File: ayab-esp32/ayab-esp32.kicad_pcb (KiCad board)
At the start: 4 copper layers, 285.1 x 48.1 mm, 237 parts, among them J201 SPARE1, J202 SPARE0, J401 900.965.CK35 SOLENOIDS A, J402 900.965.CK35 SOLENOIDS B, J403 910.950 SOLENOIDS A, J404 910.950 SOLENOIDS B, J405 910.950 ENCODERS EOL R, J406 930.940 SOLENOIDS A, J407 930.940 SOLENOIDS B, J408 910.950 EOL L, J409 930.940 EOL R, J410 930.940 ENCODERS, J411 900.965 EOL L, J412 900.965 EOL R, J413 900.965 ENCODERS, J414 930.940 EOL L, J501 USB_C_Receptacle_USB2.0, J601 VIN, J602 Brother_5P, J604 Brother_4R, J701 CTRL_3v3, J702 CTRL_5V, J801 AYAB_UART, J802 I2C_VBUS, J803 USER_I2C, J804 I2C_VBUS, J805 AYAB_SPI, J806 AYAB_I2C, Q201 AO3400A, Q501 BCM857BV, Q502 LP9435LT1G, Q801 AO3400A, Q802 AO3400A, Q803 AO3400A, Q804 AO3400A, Q805 LP9435LT1G, Q806 AO3400A, SW201 USER, SW202 RESET, SW203 BOOTSEL, U201 ESP32-S3-MINI-1, U301 MCP23017_SS, U302 ULN2003A, U303 ULN2003A, U304 ULN2003A, U403 LM66100DCKR, U501 SRV05-4, U601 XL1509, U602 XL1509, U701 SN74LVC4245

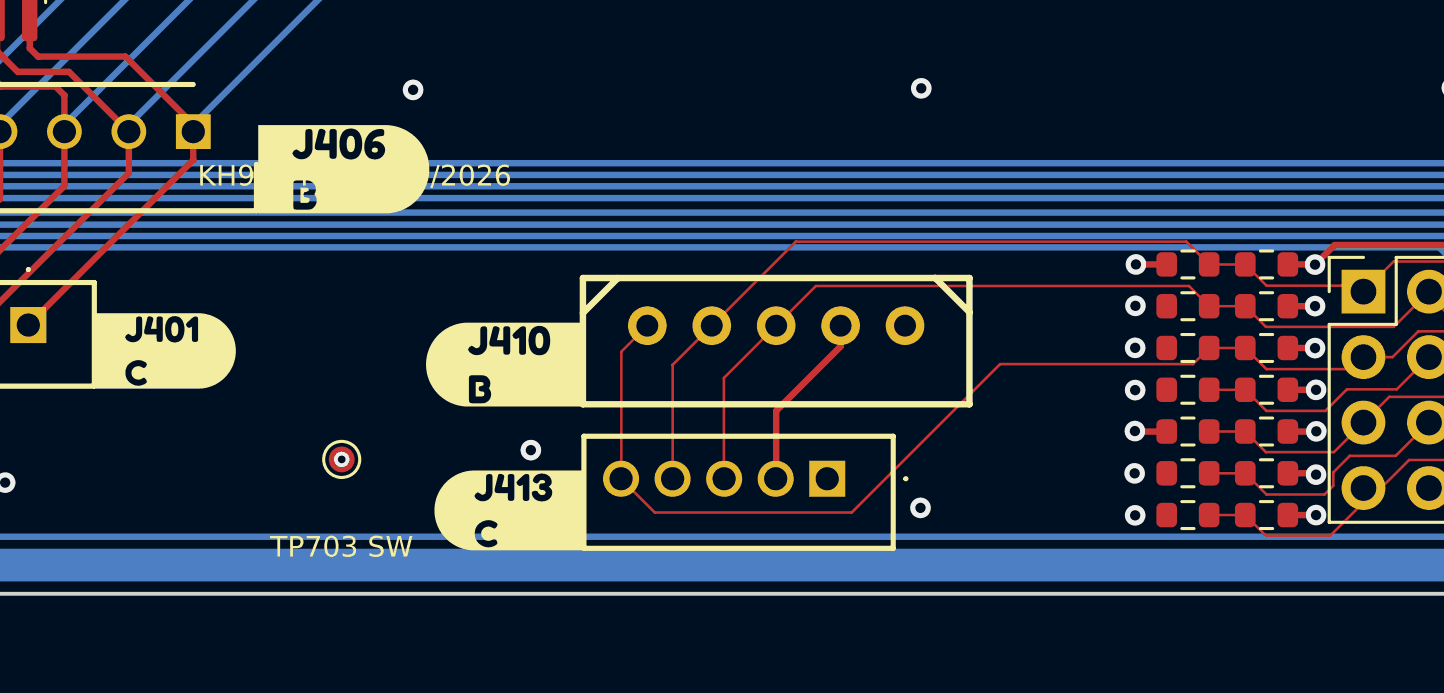
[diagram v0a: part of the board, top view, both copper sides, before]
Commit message: Close final Rev A preorder audit findings
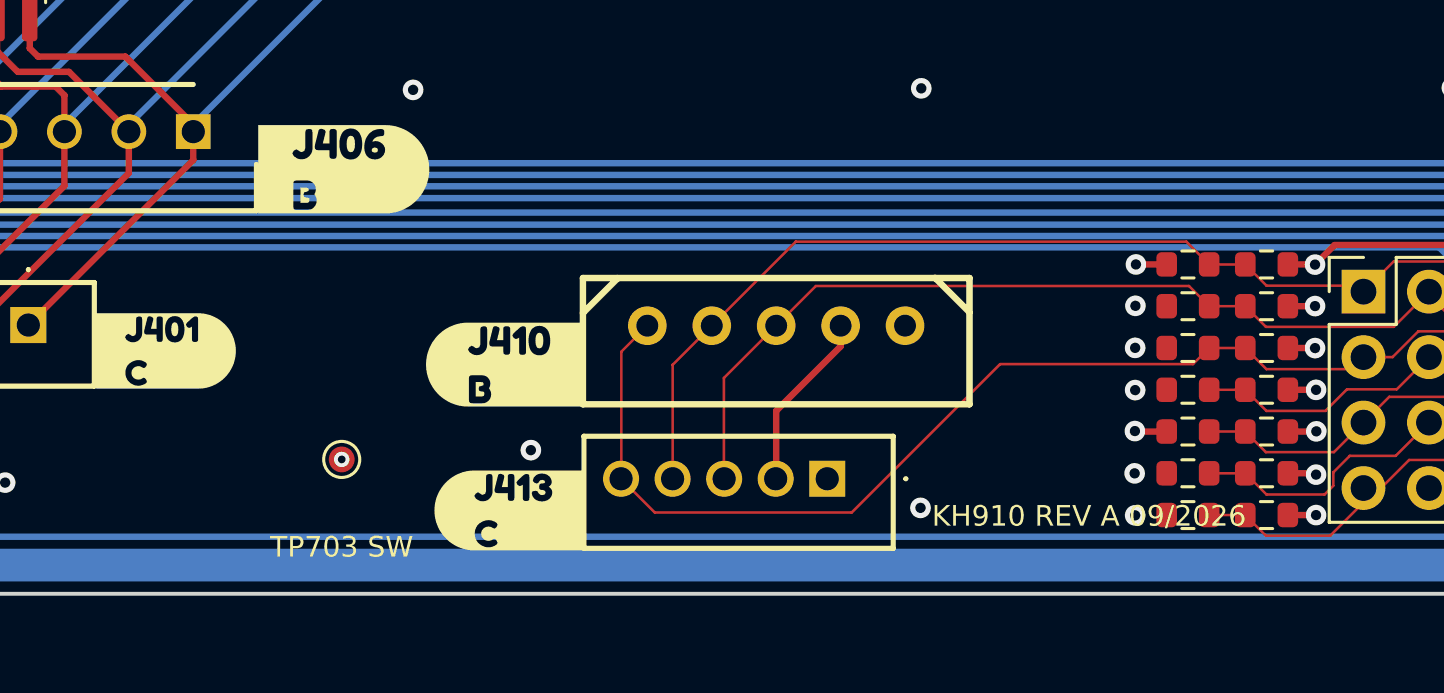
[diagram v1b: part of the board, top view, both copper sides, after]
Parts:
- H101, H102, H103, H104, H106, H108: value M3 -> M2

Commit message: Close final preorder audit blockers
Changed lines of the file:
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@@
 	)
 	(gr_text "KH910 REV A 09/2026"
-		(at 174 161.2 0)
+		(at 180 142 0)
 		(layer "F.SilkS")
 		(effects
